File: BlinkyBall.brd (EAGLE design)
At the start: 30 x 30 mm, 23 parts, among them J1 M02PTH, U1 Tiny85-20-SMT

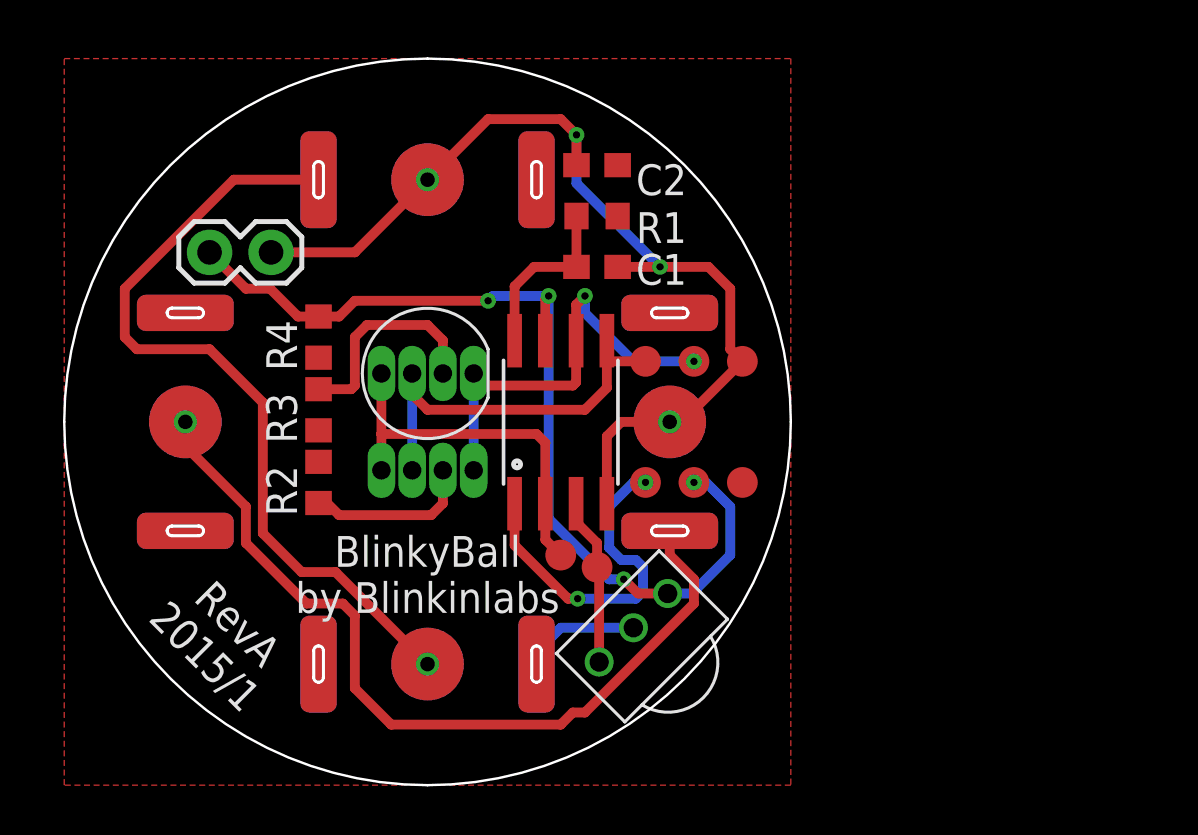
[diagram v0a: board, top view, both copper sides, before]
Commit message: Working towards RevB board design: Smaller, more vertical
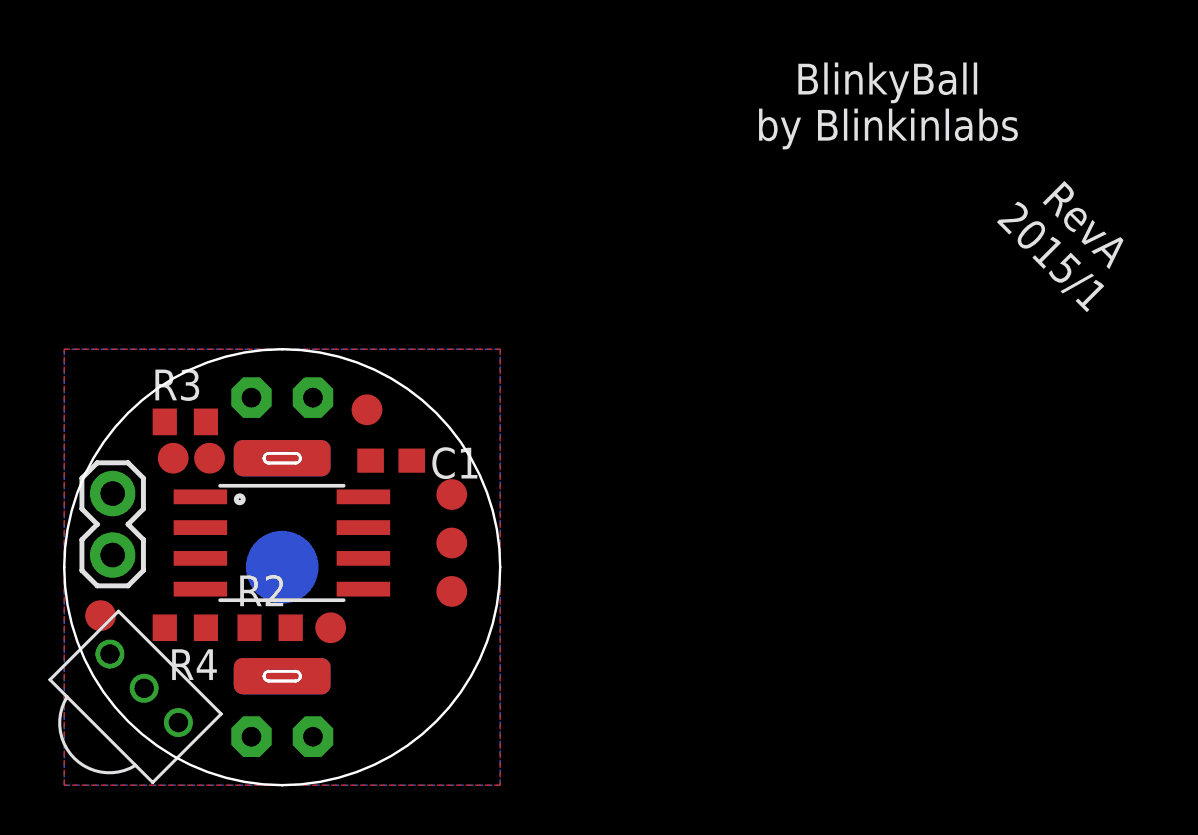
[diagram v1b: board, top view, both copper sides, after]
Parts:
- removed C2: 1uF, adafruit:C0603
- removed D1, D2: LED-RGB-CA-THRUDIFFUSE, blinkinlabs:LED-RGB-THRU
- removed R1: 10, adafruit:R0603
- removed U$1, U$3, U$4: BATTERY_BUTTON_CELLAG3-REVERSABLE, blinkinlabs:BATTERY_COVER_AG3_REVERSABLE
- added LED_BOT, LED_TOP: (no value), adafruit:LED5MM
- U$2: value BATTERY_BUTTON_CELLAG3-REVERSABLE -> BATTERY_BUTTON_CELLAG3; device blinkinlabs:BATTERY_COVER_AG3_REVERSABLE -> blinkinlabs:BATTERY_COVER_AG3
- moved TP7 20.6 mm to (1.50, 7.00)
- moved U$5 20.4 mm to (3.30, 4.00), turned to 315 degrees
- moved TP5 20.2 mm to (11.0, 6.50)
- moved TP6 18.0 mm to (6.00, 13.5)
- moved U$2 17.1 mm to (9.00, 9.00)
- moved TP8 16.5 mm to (4.50, 13.5)
- moved TP4 15.8 mm to (12.5, 15.5)
- moved R4 13.2 mm to (5.00, 6.50), turned to 0 degrees
- moved J1 13.1 mm to (2.00, 9.50), turned to 90 degrees
- moved U1 12.5 mm to (9.00, 10.0), turned to 270 degrees
- moved TP2 12.5 mm to (16.0, 10.0)
- moved TP1 12.4 mm to (16.0, 8.00)
- moved C1 11.7 mm to (13.5, 13.4)
- moved TP3 10.0 mm to (16.0, 12.0)
- moved R2 6.32 mm to (8.50, 6.50), turned to 180 degrees
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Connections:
- net N$4 renamed RESET
- removed net BLUE: D1.4, D2.4, TP8.P$1, U1.2
- removed net GREEN: D1.3, D2.3, TP1.P$1, U1.5
- removed net N$1: U$1.-1, U$1.-2, U$2.+1, U$2.+2, U$2.+3, U$2.+4
- removed net N$2: U$3.-1, U$3.-2, U$4.+1, U$4.+2, U$4.+3, U$4.+4
- removed net N$3: C1.1, R1.2, U1.8
- removed net N$8: D2.2, R2.2
- removed net N$9: D1.2, R3.2
- removed net RED: D1.1, D2.1, TP2.P$1, U1.6
- new net LED_BOTTOM: LED_BOT.A, TP1.P$1, U1.5
- new net LED_TOP: LED_TOP.A, TP2.P$1, U1.6
- new net N$4: LED_TOP.K, R3.2
- new net N$5: LED_BOT.K, R2.2
- new net XXXXX: TP8.P$1, U1.2
- net GND: now also R2.1, R3.1, U$2.-; no longer C2.2, U$2.-1, U$2.-2, U$4.-1, U$4.-2
- net V_BATT: now also C1.1, U$2.+1, U$2.+2, U$2.+3, U$2.+4, U1.8; no longer C2.1, R1.1, R2.1, R3.1, U$1.+1, U$1.+2, U$1.+3, U$1.+4, U$3.+1, U$3.+2, U$3.+3, U$3.+4
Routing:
- net GND: track 43.2 -> 0.00 mm, vias 4 -> 0
- net WAKEUP: track 39.9 -> 0.00 mm, vias 4 -> 0
- net N$1: track 34.9 -> 0.00 mm, vias 1 -> 0
- net N$2: track 33.1 -> 0.00 mm, vias 1 -> 0
- net RED: track 18.2 -> 0.00 mm, vias 2 -> 0
- net GREEN: track 17.1 -> 0.00 mm
- net BLUE: track 15.8 -> 0.00 mm
- net RESET: track 14.4 -> 0.00 mm, vias 2 -> 0
- net N$9: track 9.03 -> 0.00 mm
- net N$3: track 7.23 -> 0.00 mm
- net IR_SIGNAL: track 7.20 -> 0.00 mm
- net N$8: track 6.91 -> 0.00 mm
- net V_BATT: track 4.91 -> 0.00 mm
- added copper zone on layer 16, net GND
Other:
- board size 30 x 30 mm -> 18 x 18 mm

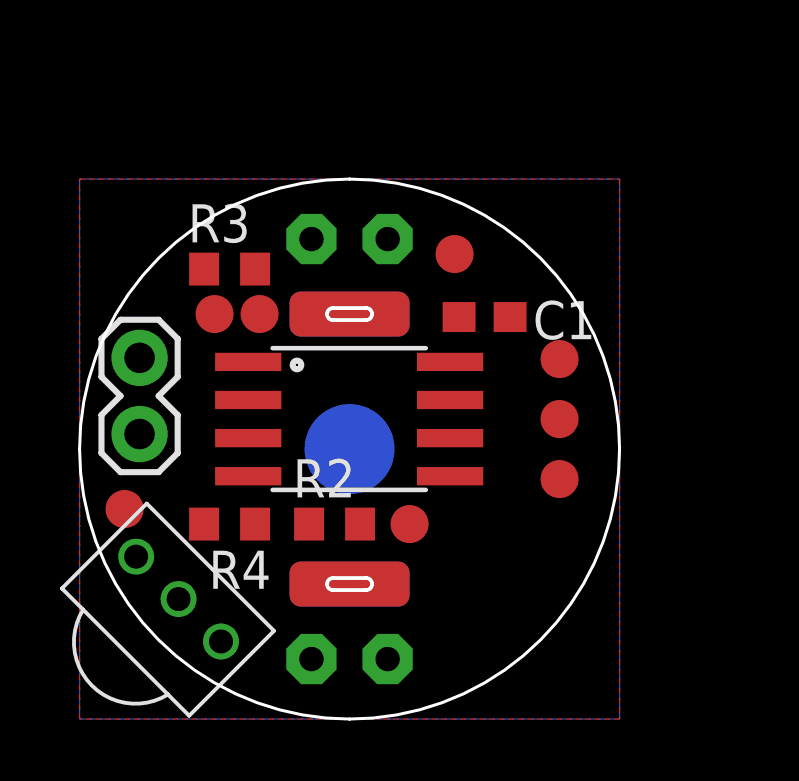
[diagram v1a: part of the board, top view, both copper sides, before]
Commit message: RevB pcb- transistor switch for LEDs
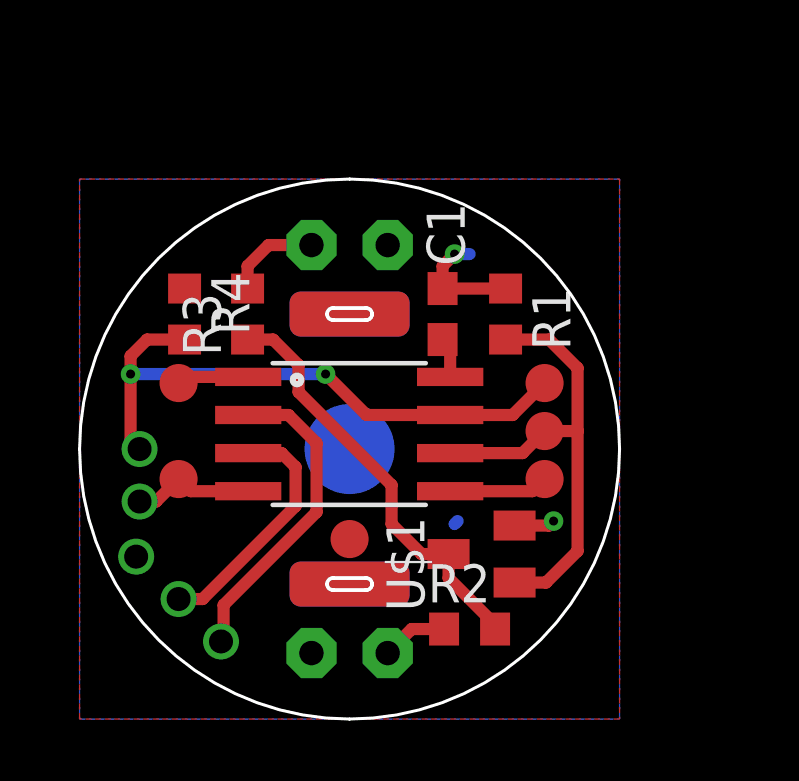
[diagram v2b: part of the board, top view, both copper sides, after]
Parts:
- removed J1: M02PTH, SparkFun-Connectors:1X02
- removed TP7, TP8: TEST-POINT3X5, SparkFun-Passives:PAD.03X.05
- added R1: 10k, adafruit:R0603
- added U$1: AO3418, blinkinlabs:SOT23
- added U$3: SW-18015P, blinkinlabs:SW-18015P
- moved TP4 10.1 mm to (9.00, 6.00)
- moved TP5 7.84 mm to (3.30, 8.00)
- moved R4 7.16 mm to (3.50, 13.5), turned to 90 degrees
- moved R2 5.70 mm to (13.0, 3.00)
- moved TP6 3.55 mm to (3.30, 11.2)
- moved R3 1.62 mm to (5.60, 13.5), turned to 90 degrees
- moved C1 1.40 mm to (12.1, 13.5), turned to 90 degrees
- moved TP3 0.94 mm to (15.5, 11.2)
- moved TP2 0.64 mm to (15.5, 9.60)
- moved TP1 0.50 mm to (15.5, 8.00)
- moved U1 0.50 mm to (9.00, 9.50)
- moved LED_BOT 0.20 mm to (9.00, 2.20), turned to 180 degrees
- moved LED_TOP 0.20 mm to (9.00, 15.8)
- flipped U$5 to the bottom, turned to 45 degrees
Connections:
- removed net LED_BOTTOM: LED_BOT.A, TP1.P$1, U1.5
- removed net XXXXX: TP8.P$1, U1.2
- new net IR_ENABLE: U$5.P$2, U1.3
- new net N$4: R2.1, R3.1, U$1.3
- new net YYYYY: TP1.P$1, U1.5
- net GND: now also R1.1, U$1.2, U$3.P$2, U$5.P$3; no longer J1.2, R2.1, R3.1
- net IR_SIGNAL: now also U1.2; no longer TP7.P$1, U1.3
- net LED_TOP: now also R1.2, U$1.1; no longer LED_TOP.A
- net V_BATT: now also LED_BOT.A, LED_TOP.A; no longer U$5.P$2
- net WAKEUP: now also U$3.P$1; no longer J1.1, U$5.P$3
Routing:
- net WAKEUP: track 0.00 -> 20.1 mm, vias 0 -> 2
- net LED_TOP: track 0.00 -> 16.0 mm
- net N$4: track 0.00 -> 14.1 mm
- net IR_SIGNAL: track 0.00 -> 10.6 mm
- net GND: track 0.00 -> 9.52 mm, vias 0 -> 2
- net IR_ENABLE: track 0.00 -> 8.25 mm
- net YYYYY: track 0.00 -> 3.31 mm
- net N$3: track 0.00 -> 3.17 mm
- net RESET: track 0.00 -> 2.41 mm
- net N$2: track 0.00 -> 2.21 mm
- net V_BATT: track 0.00 -> 1.35 mm
